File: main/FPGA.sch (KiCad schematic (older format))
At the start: 43 parts

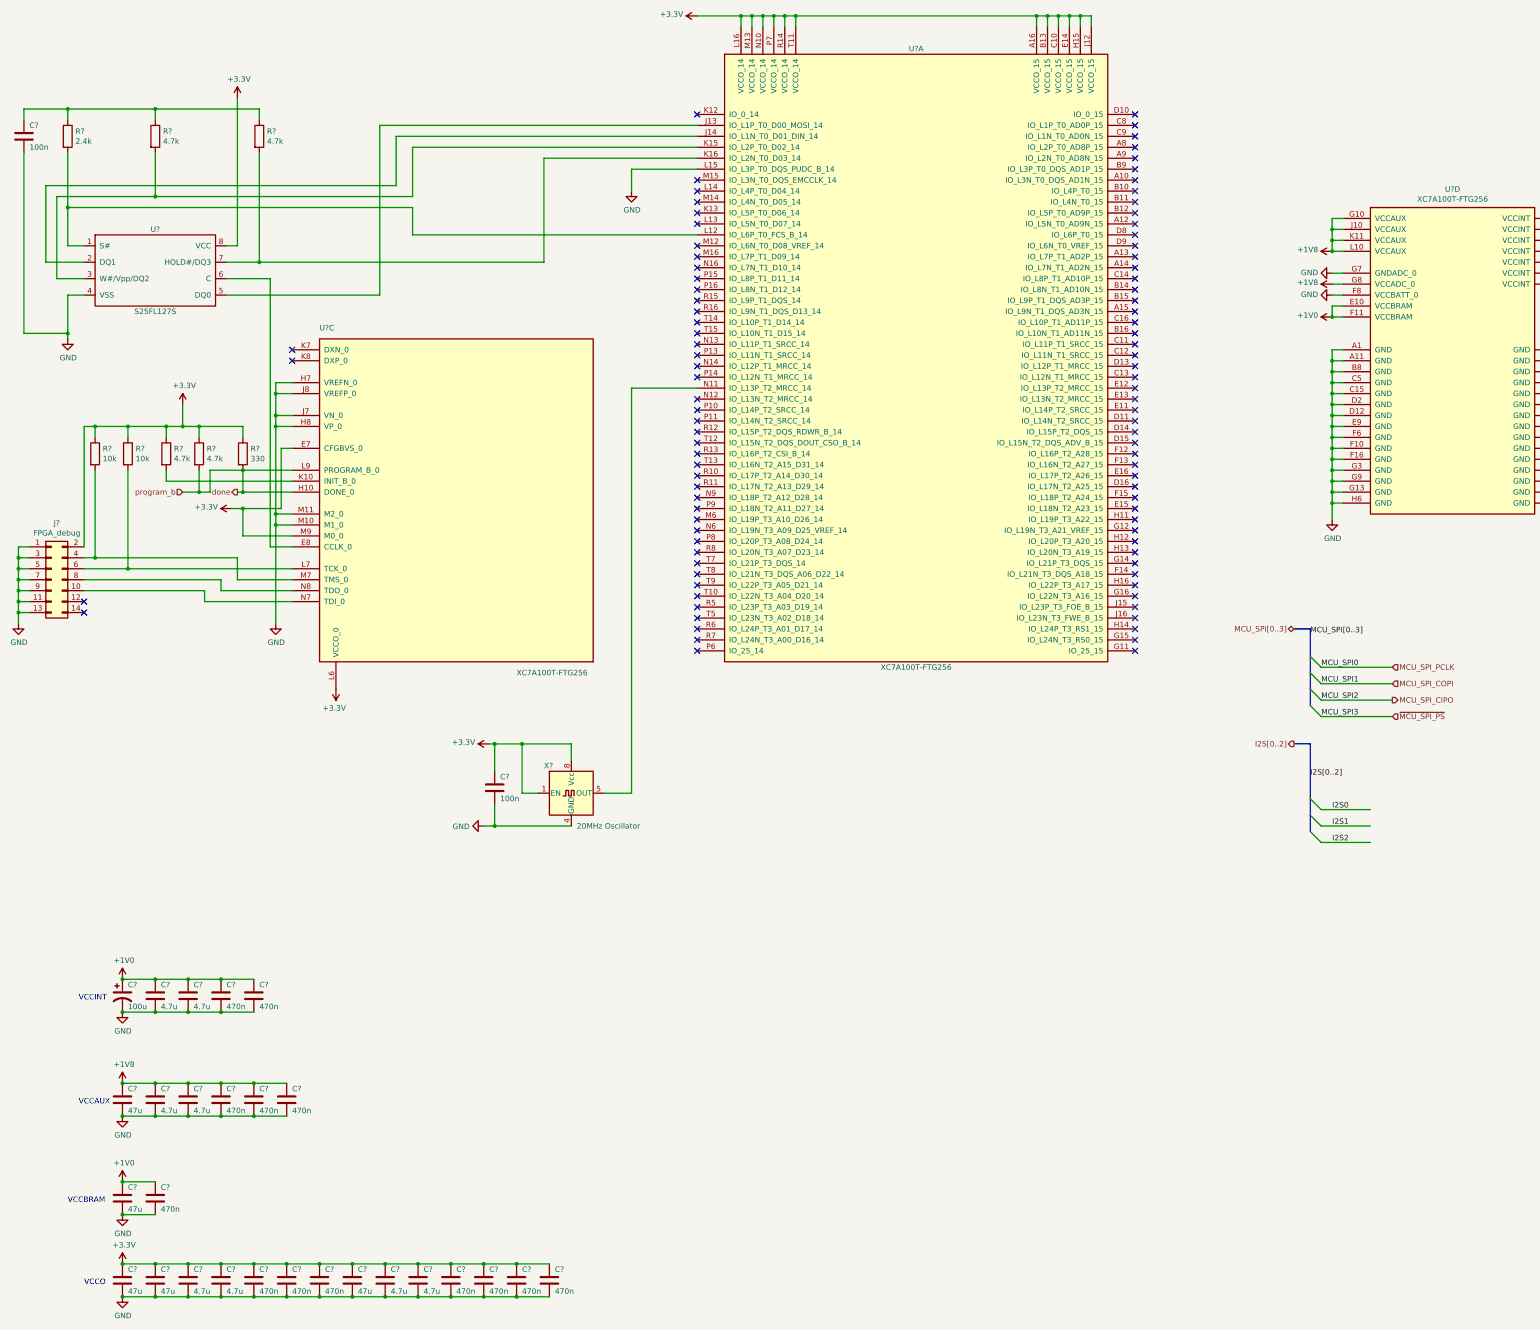
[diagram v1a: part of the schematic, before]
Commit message: Set up switching regulator circuits.
We only use half of the switching regulator that generates the 1V0
voltage. I'm not sure if the half not being used is connected correctly.
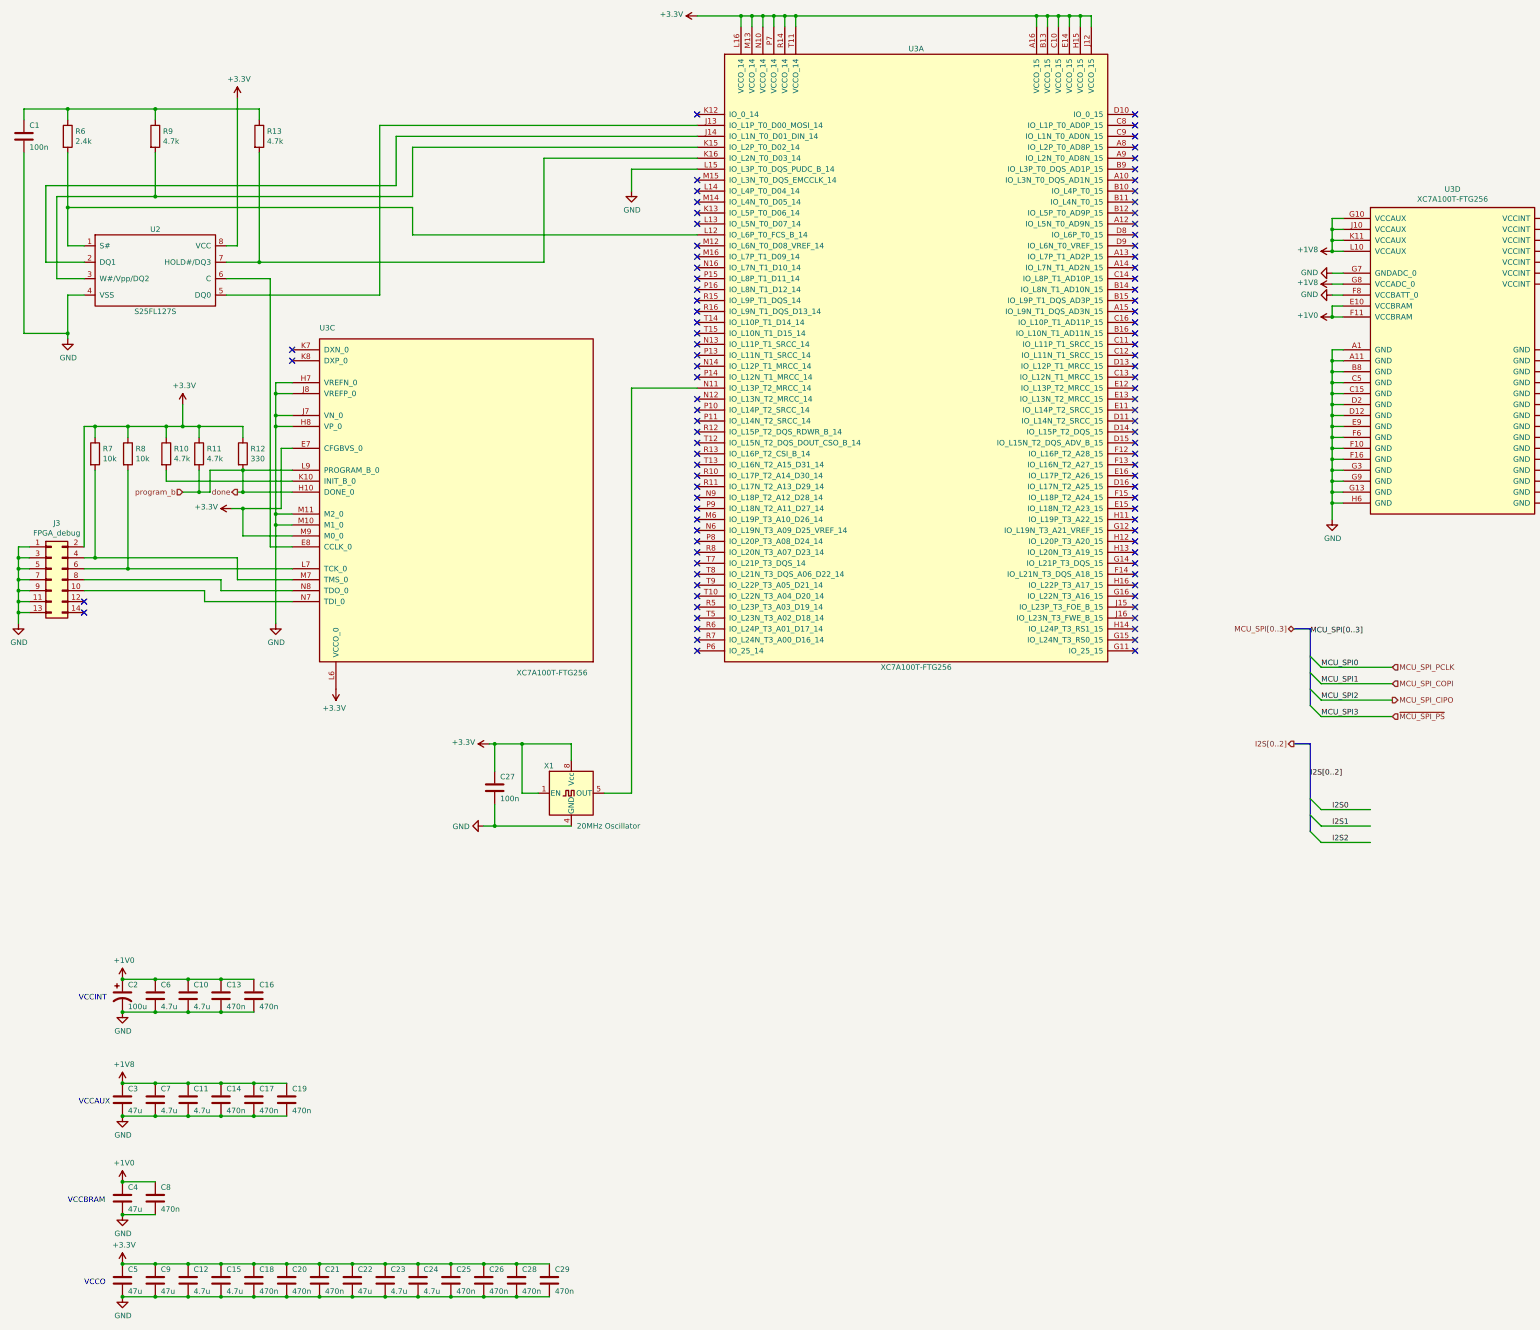
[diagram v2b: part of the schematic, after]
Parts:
- gave numbers to parts that had none: 41

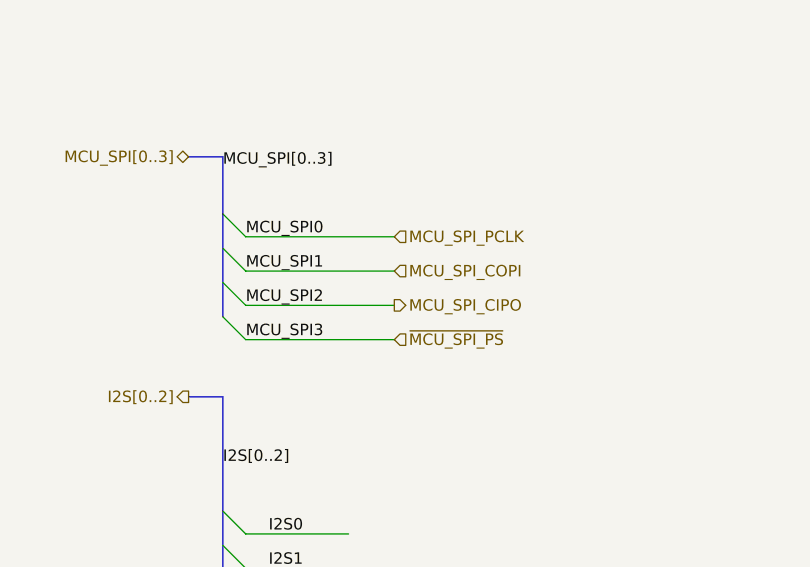
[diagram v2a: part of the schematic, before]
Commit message: Continue wiring of the MCU
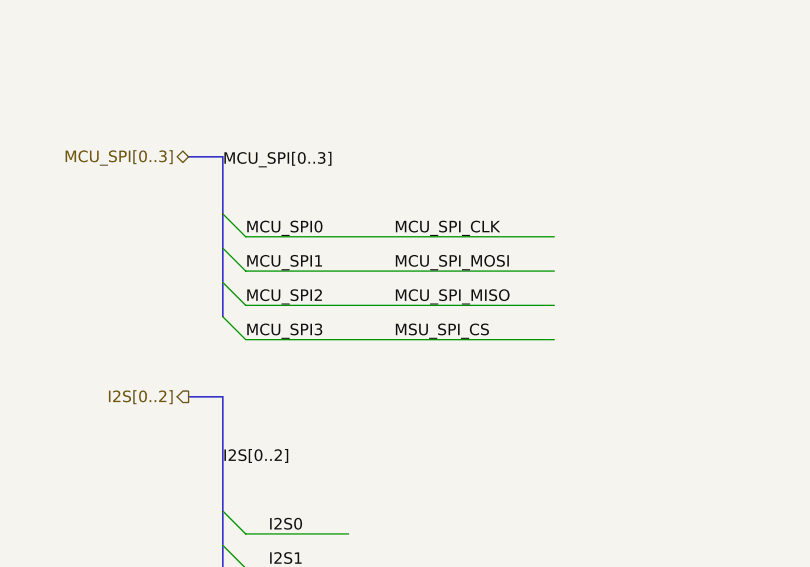
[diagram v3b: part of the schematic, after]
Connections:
- net labels added: MCU_SPI_CLK, MCU_SPI_MISO, MCU_SPI_MOSI, MSU_SPI_CS
- net labels removed: MCU_SPI_CIPO, MCU_SPI_COPI, MCU_SPI_PCLK, ~MCU_SPI_PS
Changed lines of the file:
@@
 $Descr A2 23386 16535
 encoding utf-8
-Sheet 3 7
+Sheet 7 7
 Title "Audio project FPGA connections"
 Date ""
@@
 Entry Wire Line
 	12500 7550 12600 7650
-Text HLabel 13250 8100 2    50   Input ~ 0
-~MCU_SPI_PS
-Text HLabel 13250 7950 2    50   Output ~ 0
-MCU_SPI_CIPO
-Text HLabel 13250 7800 2    50   Input ~ 0
-MCU_SPI_COPI
-Text HLabel 13250 7650 2    50   Input ~ 0
-MCU_SPI_PCLK
 Text Label 12500 7350 0    50   ~ 0
 MCU_SPI[0..3]
@@
 MCU_SPI3
 Wire Wire Line
-	12600 7650 13250 7650
-Wire Wire Line
-	12600 7800 13250 7800
-Wire Wire Line
-	12600 7950 13250 7950
-Wire Wire Line
-	12600 8100 13250 8100
+	12600 7800 13950 7800
+Wire Wire Line
+	12600 7950 13950 7950
+Wire Wire Line
+	12600 8100 13950 8100
 Entry Wire Line
 	12500 9150 12600 9250
@@
 NoConn ~ 10900 2600
 NoConn ~ 10900 2900
+Wire Wire Line
+	12600 7650 13950 7650
+Text Label 13250 7650 0    50   ~ 0
+MCU_SPI_CLK
+Text Label 13250 7800 0    50   ~ 0
+MCU_SPI_MOSI
+Text Label 13250 7950 0    50   ~ 0
+MCU_SPI_MISO
+Text Label 13250 8100 0    50   ~ 0
+MSU_SPI_CS
 Wire Bus Line
 	12500 8350 12500 9150

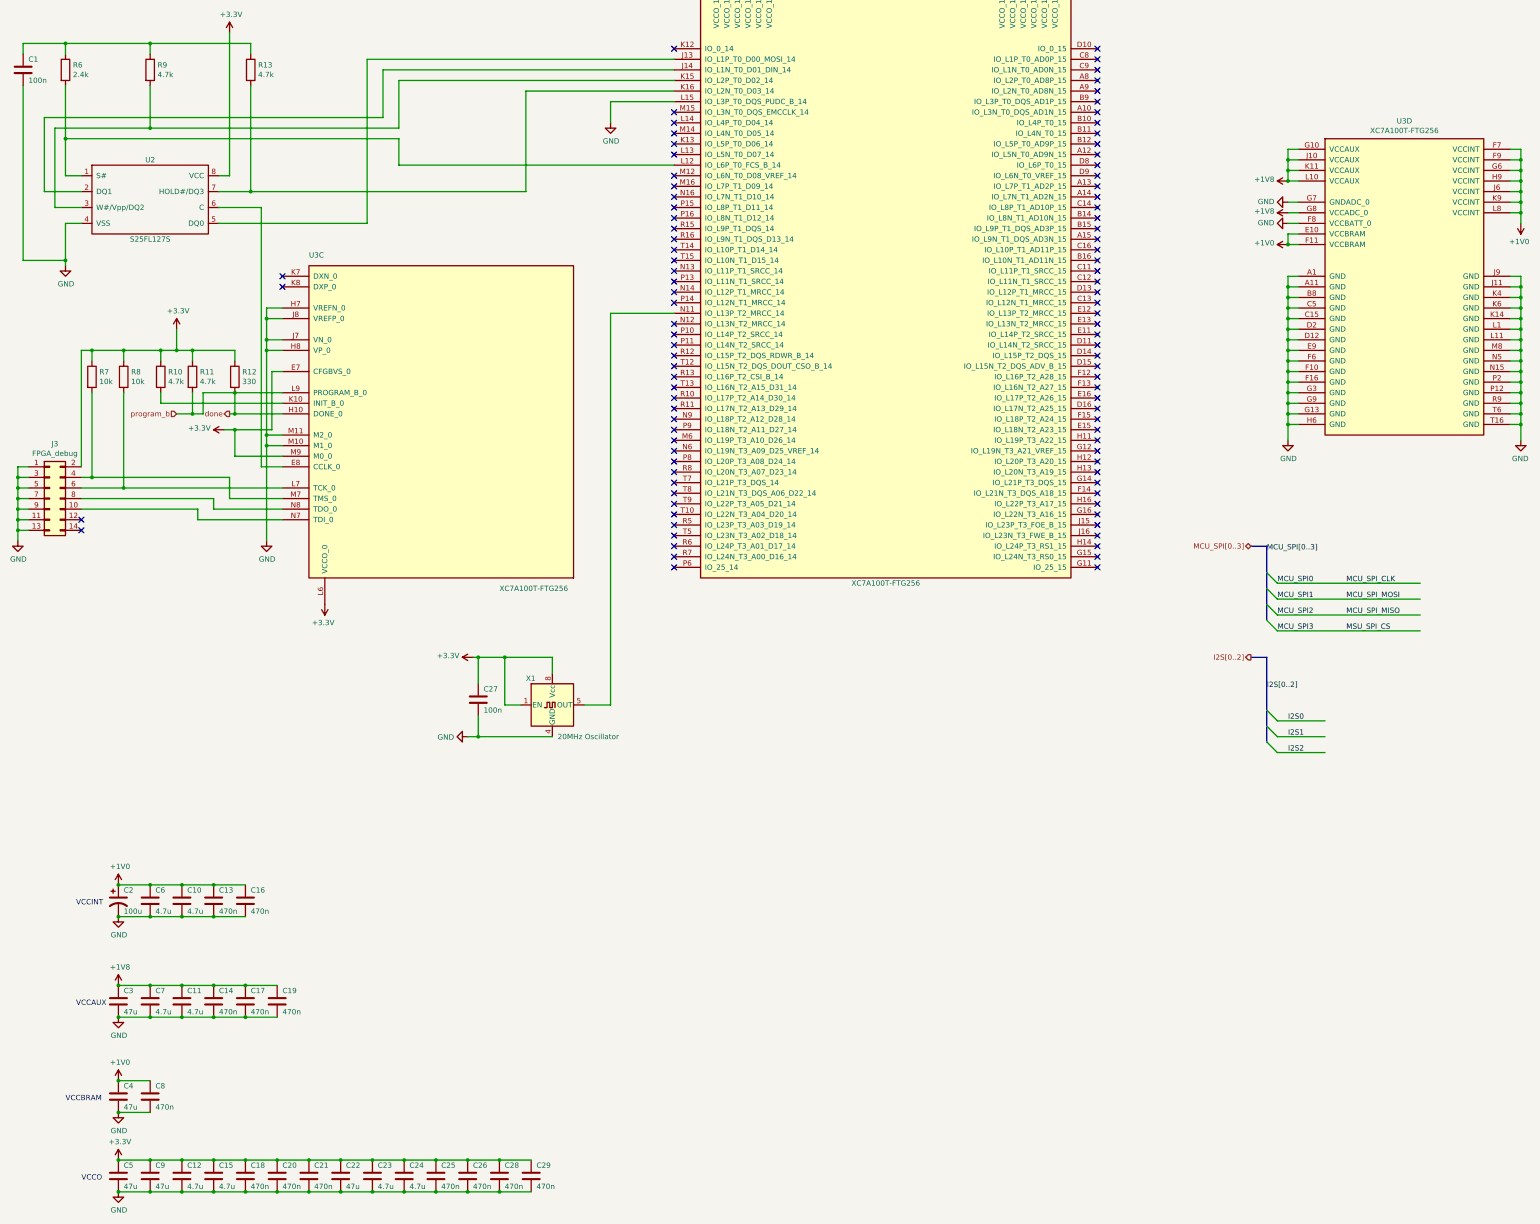
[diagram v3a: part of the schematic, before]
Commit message: Be consistent with capacitor values (always use F)
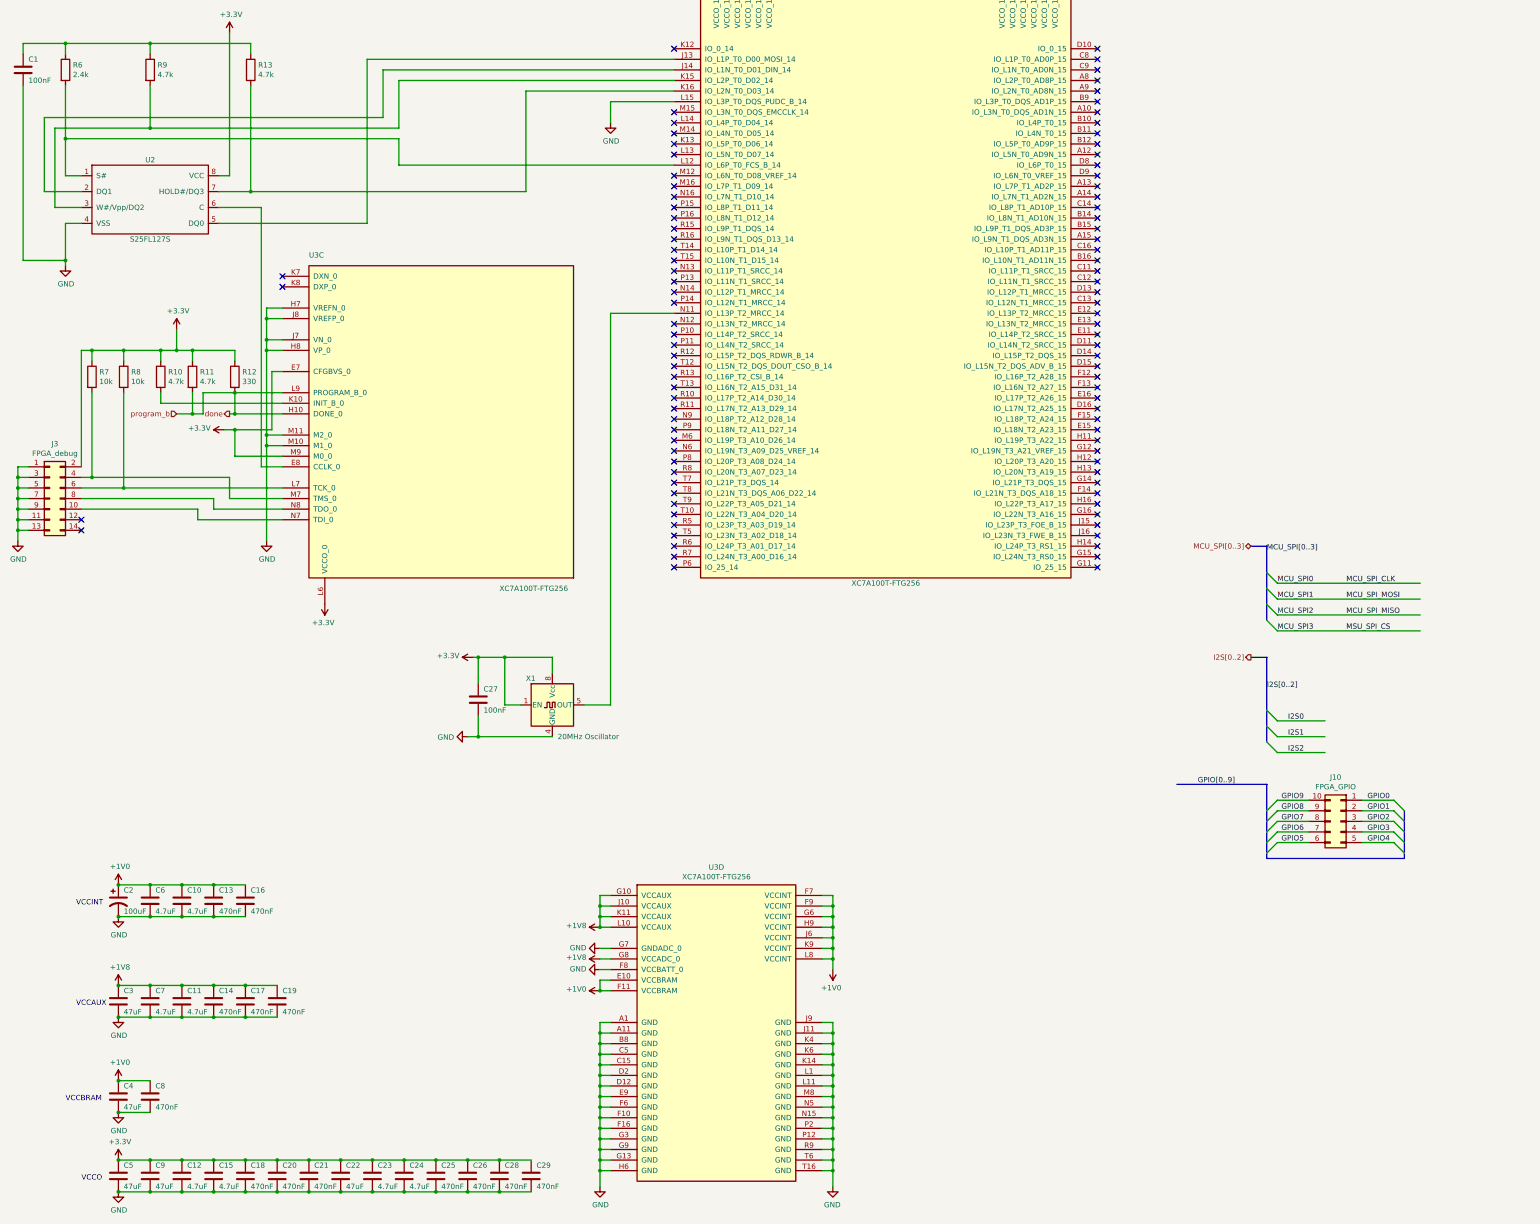
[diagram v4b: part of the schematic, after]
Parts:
- added J10: FPGA_GPIO, symbol Connector_Generic:Conn_02x05_Counter_Clockwise
- C1, C27: value 100n -> 100nF
- C10, C11, C12, C15, C23, C24, C6, C7: value 4.7u -> 4.7uF
- C13, C14, C16, C17, C18, C19, C20, C21, C25, C26, C28, C29, C8: value 470n -> 470nF
- C2: value 100u -> 100uF
- C22, C3, C4, C5, C9: value 47u -> 47uF
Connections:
- net labels added: GPIO0, GPIO1, GPIO2, GPIO3, GPIO4, GPIO5, GPIO6, GPIO7, GPIO8, GPIO9, GPIO[0..9]
- wire segments 292 -> 302
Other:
- moved on the sheet: U3D

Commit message: FPGA connections, DAC linear regulator removed, DAC I2S breakout
Connected the SPI, I2S and GPIO to some (mostly) arbitrary pins. Notably
the SPI clock has to be connected to a clock pin on the FPGA.

The linear regulator is (hopefully) not needed for the DAC as we already
have a separate analog +3.3V created by the switching regulators.

The I2S wires to the DAC are now connected to the FPGA as well as
breakout pins over 0 ohm resistors, in case we need to connect to an
external FPGA.
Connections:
- net GPIO0: now also U3.R7 (IO_L24N_T3_A00_D16_14)
- net GPIO1: now also U3.R6 (IO_L24P_T3_A01_D17_14)
- net GPIO2: now also U3.T5 (IO_L23N_T3_A02_D18_14)
- net GPIO3: now also U3.R5 (IO_L23P_T3_A03_D19_14)
- net GPIO4: now also U3.T10 (IO_L22N_T3_A04_D20_14)
- net GPIO5: now also U3.T9 (IO_L22P_T3_A05_D21_14)
- net GPIO6: now also U3.T8 (IO_L21N_T3_DQS_A06_D22_14)
- net GPIO7: now also U3.T7 (IO_L21P_T3_DQS_14)
- net GPIO8: now also U3.R8 (IO_L20N_T3_A07_D23_14)
- net GPIO9: now also U3.P8 (IO_L20P_T3_A08_D24_14)
- net I2S0: now also U3.M16 (IO_L7P_T1_D09_14)
- net I2S1: now also U3.N16 (IO_L7N_T1_D10_14)
- net I2S2: now also U3.P15 (IO_L8P_T1_D11_14)
- net MCU_SPI0: now also U3.N12 (IO_L13N_T2_MRCC_14)
- net MCU_SPI1: now also U3.T13 (IO_L16N_T2_A15_D31_14)
- net MCU_SPI2: now also U3.R10 (IO_L17P_T2_A14_D30_14)
- net MCU_SPI3: now also U3.R11 (IO_L17N_T2_A13_D29_14)
- no-connect marks 97 -> 80
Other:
- moved on the sheet: C1, C10, C11, C12, C13, C14, C15, C16, C17, C18, C19, C2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
